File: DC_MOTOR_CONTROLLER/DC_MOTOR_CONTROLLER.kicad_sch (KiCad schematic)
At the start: 0 parts

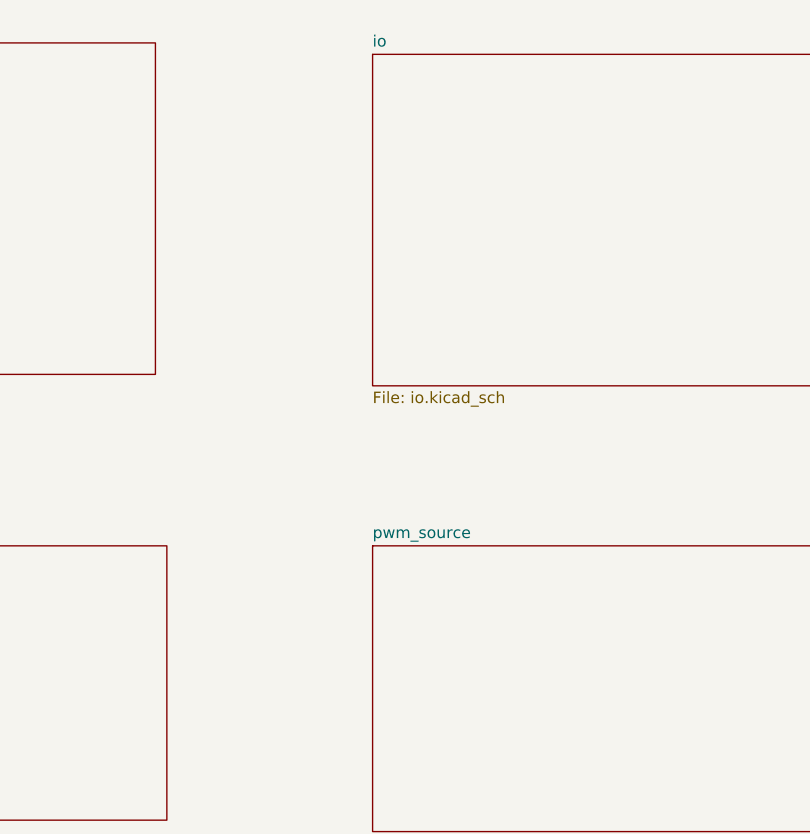
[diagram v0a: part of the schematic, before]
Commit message: worked on h-bridge, pwm, io
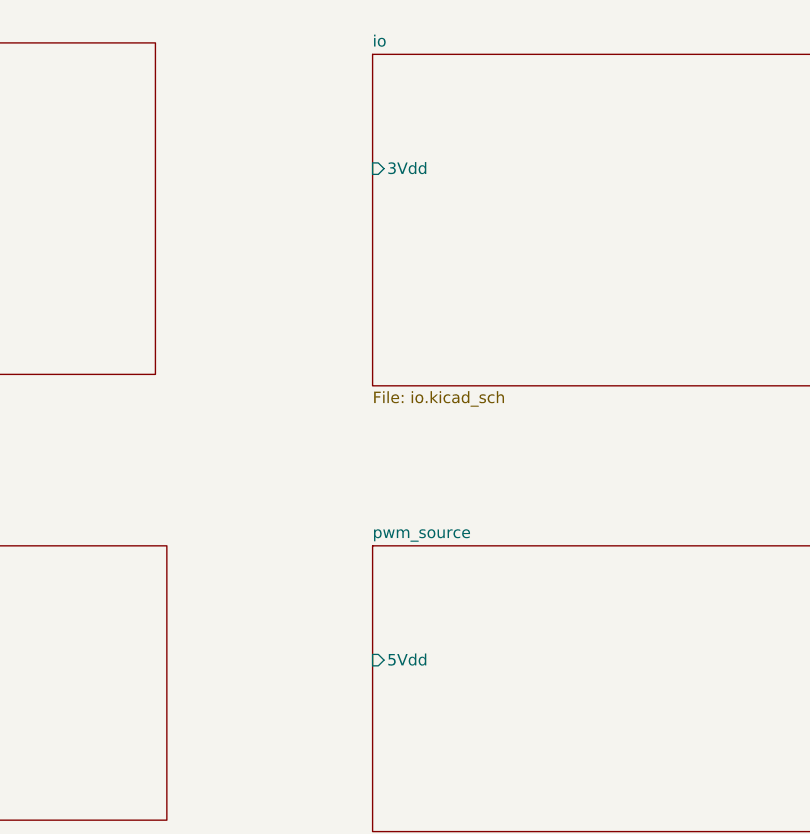
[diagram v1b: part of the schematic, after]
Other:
- sheet io ports: added 3Vdd; removed none
- sheet pwm_source ports: added 5Vdd; removed none
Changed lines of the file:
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@@
+			)
+		)
+		(pin "3Vdd" input
+			(at 111.76 35.56 180)
+			(effects
+				(font
+					(size 1.27 1.27)
+				)
+				(justify left)
 			)
 		)
@@
 			)
 		)
+		(pin "5Vdd" input
+			(at 111.76 90.17 180)
+			(effects
+				(font
+					(size 1.27 1.27)
+				)
+				(justify left)
+			)
+		)
